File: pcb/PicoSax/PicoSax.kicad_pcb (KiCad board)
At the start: 2 copper layers, 100 x 160 mm, 80 parts, among them J3 Conn_01x02, M1 MountingHole_3.2mm_M3, M2 MountingHole_3.2mm_M3, M3 MountingHole_3.2mm_M3, M4 MountingHole_3.2mm_M3, M5 MountingHole_3.2mm_M3, M6 MountingHole_3.2mm_M3, SW8va1 Omron_B3K_L13L, SW8vb1 Omron_B3K_L13L, U1 Perfboard

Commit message: Clean and Parts BOM
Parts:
- R16: footprint Resistor_THT:R_Axial_DIN0204_L3.6mm_D1.6mm_P7.62mm_Horizontal -> Resistor_SMD:R_1210_3225Metric_Pad1.30x2.65mm_HandSolder
- R17: footprint Resistor_THT:R_Axial_DIN0204_L3.6mm_D1.6mm_P7.62mm_Horizontal -> Resistor_SMD:R_0805_2012Metric_Pad1.20x1.40mm_HandSolder
- moved R16 20.9 mm to (138.0, 187.0), turned to -90 degrees
- moved R17 3.31 mm to (123.0, 201.5)
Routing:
- net +3V3: track 450.2 -> 441.0 mm, vias 1 -> 2
- net Net-(J2-Vref): track 9.94 -> 4.78 mm
- net Net-(A1-GPIO0): track 14.7 -> 17.2 mm
- net Net-(J2-Data): track 9.94 -> 12.2 mm

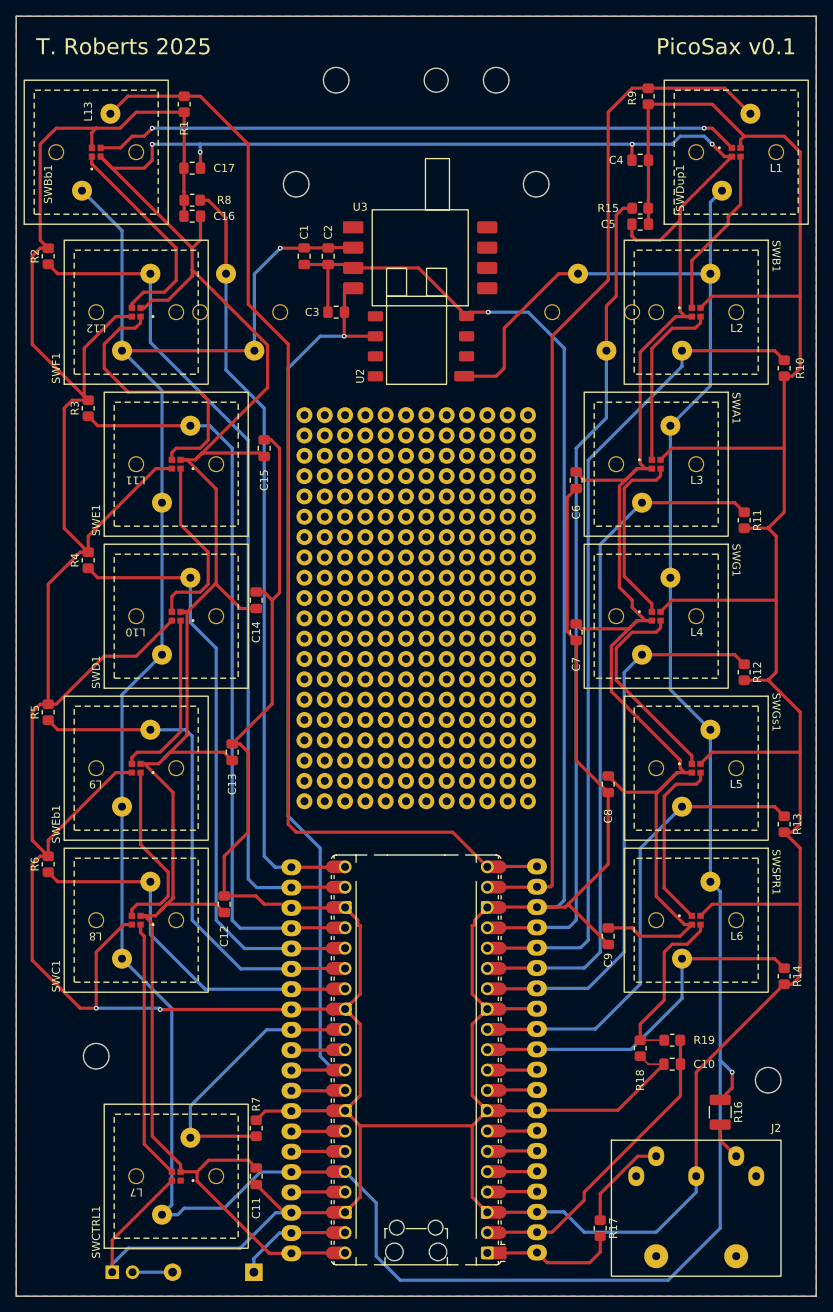
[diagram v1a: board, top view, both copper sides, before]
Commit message: v0.2
Updated LED footprint to have correct pin numbering.  Redid layout and traces. Added helpful silkscreen for pi pico.  Added some datasheets.
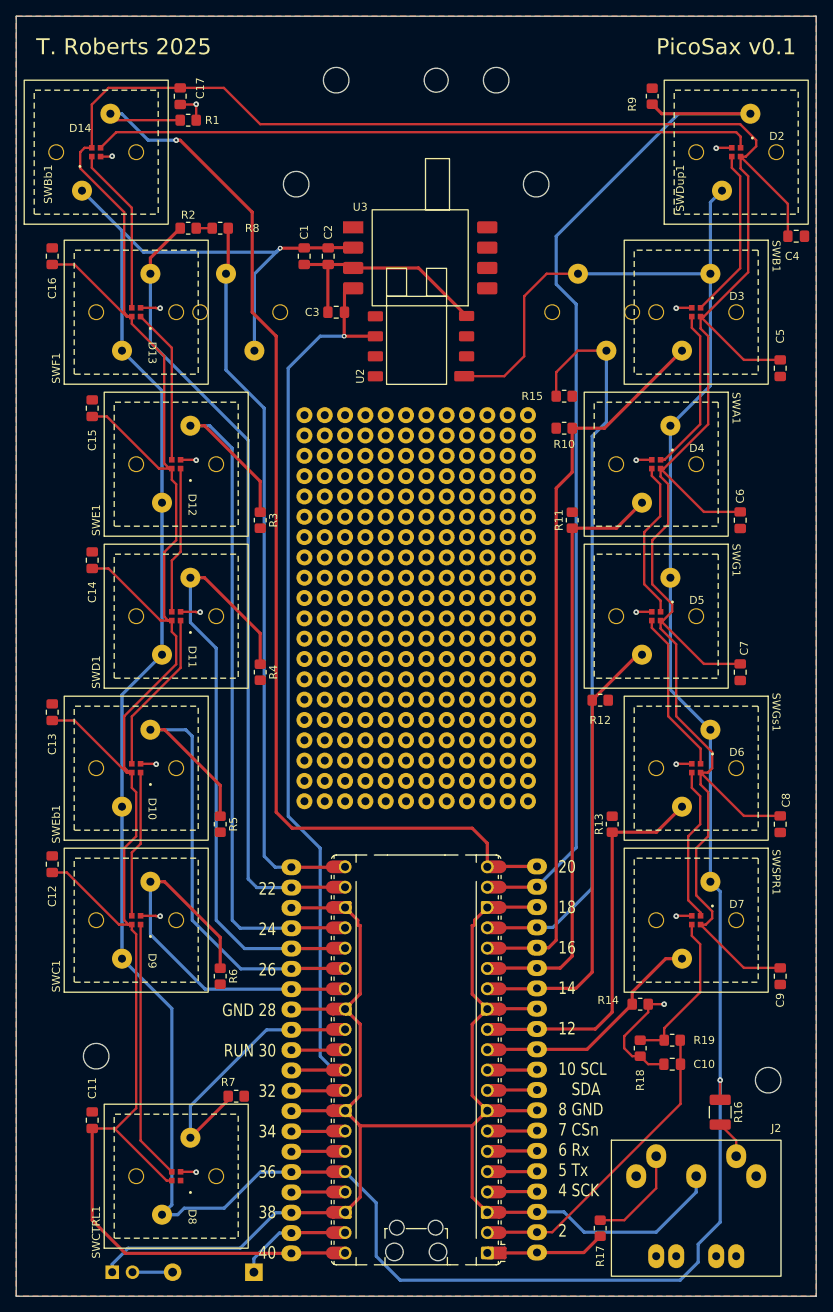
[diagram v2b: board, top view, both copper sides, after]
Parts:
- D10: renamed from L9; footprint MyLibrary:19-C47&slash_RSGHBHC-5V01&slash_2T_EVE-M -> PicoSax:19-C47_RSGHBHC-5V01-2T
- D11: renamed from L10; footprint MyLibrary:19-C47&slash_RSGHBHC-5V01&slash_2T_EVE-M -> PicoSax:19-C47_RSGHBHC-5V01-2T
- D12: renamed from L11; footprint MyLibrary:19-C47&slash_RSGHBHC-5V01&slash_2T_EVE-M -> PicoSax:19-C47_RSGHBHC-5V01-2T
- D13: renamed from L12; footprint MyLibrary:19-C47&slash_RSGHBHC-5V01&slash_2T_EVE-M -> PicoSax:19-C47_RSGHBHC-5V01-2T
- D14: renamed from L13; footprint MyLibrary:19-C47&slash_RSGHBHC-5V01&slash_2T_EVE-M -> PicoSax:19-C47_RSGHBHC-5V01-2T
- D2: renamed from L1; footprint MyLibrary:19-C47&slash_RSGHBHC-5V01&slash_2T_EVE-M -> PicoSax:19-C47_RSGHBHC-5V01-2T
- D3: renamed from L2; footprint MyLibrary:19-C47&slash_RSGHBHC-5V01&slash_2T_EVE-M -> PicoSax:19-C47_RSGHBHC-5V01-2T
- D4: renamed from L3; footprint MyLibrary:19-C47&slash_RSGHBHC-5V01&slash_2T_EVE-M -> PicoSax:19-C47_RSGHBHC-5V01-2T
- D5: renamed from L4; footprint MyLibrary:19-C47&slash_RSGHBHC-5V01&slash_2T_EVE-M -> PicoSax:19-C47_RSGHBHC-5V01-2T
- D6: renamed from L5; footprint MyLibrary:19-C47&slash_RSGHBHC-5V01&slash_2T_EVE-M -> PicoSax:19-C47_RSGHBHC-5V01-2T
- D7: renamed from L6; footprint MyLibrary:19-C47&slash_RSGHBHC-5V01&slash_2T_EVE-M -> PicoSax:19-C47_RSGHBHC-5V01-2T
- D8: renamed from L7; footprint MyLibrary:19-C47&slash_RSGHBHC-5V01&slash_2T_EVE-M -> PicoSax:19-C47_RSGHBHC-5V01-2T
- D9: renamed from L8; footprint MyLibrary:19-C47&slash_RSGHBHC-5V01&slash_2T_EVE-M -> PicoSax:19-C47_RSGHBHC-5V01-2T
- J2: footprint MyLibrary:MIDI_DIN5 -> PicoSax:MIDI_DIN5
- moved R10 28.5 mm to (118.5, 101.5), turned to 180 degrees
- moved R3 25.7 mm to (80.5, 113.0), turned to -90 degrees
- moved R4 25.7 mm to (80.5, 132.0), turned to -90 degrees
- moved R5 25.7 mm to (75.5, 151.0), turned to -90 degrees
- moved R6 25.7 mm to (75.5, 170.0), turned to -90 degrees
- moved R15 25.3 mm to (118.5, 97.5)
- moved C5 25.1 mm to (145.5, 94.0), turned to -90 degrees
- moved C13 23.0 mm to (54.5, 137.0)
- moved C12 22.1 mm to (54.5, 156.0)
- moved C15 22.1 mm to (59.5, 99.0)
- moved C8 22.1 mm to (145.5, 151.0)
- moved C9 22.1 mm to (145.5, 170.0)
- moved C4 21.7 mm to (147.5, 77.5)
- moved C11 21.7 mm to (59.5, 188.0), turned to 90 degrees
- moved R11 21.5 mm to (119.5, 113.0), turned to 90 degrees
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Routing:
- net GND: track 1029.9 -> 278.9 mm, vias 3 -> 15
- net +5V: track 498.5 -> 538.0 mm, vias 4 -> 0
- net Net-(D12-DIn): track 35.2 -> 19.5 mm
- net /Spr: track 45.2 -> 29.9 mm
- net /G: track 70.4 -> 56.6 mm
- net /B: track 104.8 -> 91.6 mm
- net /A: track 86.6 -> 74.8 mm
- net /8va: track 104.1 -> 93.5 mm
- net /Gs: track 59.1 -> 49.0 mm
- net Net-(D13-DIn): track 27.1 -> 21.0 mm
- net /F: track 106.6 -> 100.5 mm
- net /Dup: track 128.1 -> 134.0 mm
- net Net-(D5-DIn): track 25.9 -> 20.4 mm
- net /8vb: track 96.6 -> 91.3 mm
- net Net-(D11-DIn): track 23.0 -> 18.4 mm
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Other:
- board text added: "20 18 16 14 12 10 SCL SDA 8 GND 7 CSn 6 Rx 5 Tx 4 SCK 2"
- board text added: "22 24 26 GND 28 RUN 30 32 34 36 38 40"

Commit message: v0.2 Silkscreen
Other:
- board text added: "PicoSax v0.2"
- board text removed: "PicoSax v0.1"
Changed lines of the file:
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@@
 		)
 		(group ""
-			(members "086fbb49-340c-4092-ac16-3b2fb377506b" "0a748075-0325-4b25-ae1c-3b1340523989"
-				"0d9e2712-da3d-46ba-941b-578c9ca9716c" "0ec12be3-4299-4eed-8999-63e04e5bf408"
-				"14a3973c-bdbb-4f0b-ab51-99a944f14e3e" "170240d3-fe36-4ea2-aa65-822ce0f79894"
-				"248369f5-9f03-40ea-9894-73d1c22f1eb1" "2769e762-5a5d-4509-b222-9d5381171c7f"
-				"289c9828-77ef-4c7b-af1b-91fe4cccb365" "33c5214b-91d3-4bb3-9e43-7ec0733ebdd1"
-				"3e696417-7c9f-4e13-a6cd-ef270a2be7b6" "3f76528c-e8b3-4a1b-8cd7-3c9018933f79"
-				"40fea327-c866-45ed-9e40-b74438490b45" "4447463b-c720-4ec7-bba4-d10f0006f087"
-				"4be8b8df-a1cf-4da1-a25b-0f428821f060" "4d750b4a-1d82-4a57-a198-2df9849864f4"
-				"4d9647c7-de3c-47eb-9cef-4c4329a06382" "503569ec-f38e-41fd-9da8-a40785697783"
-				"54137541-2ff5-4156-8561-277d4b1860de" "56452df0-3793-4f6e-a38a-697a60366b47"
-				"5b9ee21b-1fea-46f3-b042-433d96bef95c" "60c96f77-5977-4711-baa9-736da1819767"
-				"6398b5f7-4add-428c-a507-9e618a09b480" "7085014e-72e0-4125-83da-d3b098a96abc"
-				"80594243-740f-4f1b-9363-dd562a7afe8a" "8bdffc08-4f19-4167-9494-c7daa5d9dd6e"
-				"8c683222-ecae-4a6d-a243-7c2dc7efff21" "8d99eefa-dd62-4b80-9d0e-75e5e37bdcdd"
-				"9aed28ff-c19e-4012-900c-070ae005ab42" "9af7f3ec-2d6b-43ff-a139-916a5a7395cc"
-				"9b064802-be43-4997-8182-7c9f972b9e79" "a5f9b0f7-63f7-41f4-bb60-1ae81ea60400"
-				"b00e83cc-4dd9-4ec2-87f4-2ec63945b012" "bddd0c79-6914-4cd3-b7e1-5f6f926488bf"
-				"c8f31c3e-e067-462c-b37f-ecec6f1ce858" "cb819c15-e7df-4ca2-8b22-6a7a1858fb93"
-				"d18fe79f-21fa-456b-97f7-b86b6fc3217a" "ddef6eee-512b-46bc-ac8e-7605d60f2b34"
-				"e277d9b8-fa04-4c39-99f8-5f855f8691c6" "e882dc5c-5fe6-4eba-8a98-0ab16f5c633a"
-				"e9d9d8c0-7030-4c00-acf4-5d9ab202e600" "eb0569bd-4187-4b98-8c4f-fb153d72eacf"
-				"ed551a5c-b073-43c5-9a28-df3dba0d35ab" "f1a64061-988b-4cb4-83e3-6c89f19fb58b"
-				"f3755e70-bf1c-45a8-b774-8f128797788a" "f74f5067-8940-4ee6-b594-05108584752e"
-				"f883a951-2930-40b7-8f3a-b64df69e0cfc" "fcecb49e-15f6-498d-adc9-82b7929b87a8"
-			)
-		)
-		(group ""
-			(members "0dfa6f0c-d96c-4c15-9d40-9307cf0acaf8" "1f269a71-376d-4267-bcaf-e124a14d4f1a"
-				"3366d0ed-e0c7-4618-af66-3a9920fa8abc" "369f357f-3c73-48ee-b1d9-4a2c1381d4b6"
-				"473abd8e-769c-4bb9-a4e9-b8062483d0df" "5cae54b6-ead8-47ad-8059-047de7cd318b"
-				"621a164e-f9d4-4e92-af63-c6ef2c5eeb81" "62587bbc-7df0-400b-af10-01b4adb5f2bf"
-				"790c9925-8b04-4a0d-b4ad-d7ccd3edc333" "814d9836-6b26-4b5f-babc-7e3aa374dca8"
-				"83ee131c-baf6-45b0-a961-c326a8d426d5" "8478b01e-935e-4d0c-bc6d-8d94a3b51a82"
-				"8b57397b-aa09-47d6-8941-ed0fe9d304c0" "8df7fa84-caf1-4d86-a20b-ff41820abee2"
-				"909b767e-bd7f-4e72-9072-c8ff5f8d2dfb" "94d98e94-029a-429d-9804-492ef8209813"
-				"a0af8e8c-045e-4797-889c-f621b26a09d3" "a3caeba2-1f38-4159-8037-493ff2e50467"
-				"adc18a67-06d6-4bc2-ba0f-eb59b7a19c8c" "bea10445-694b-472f-9fca-e11192d6843f"
-				"bf364228-297f-4708-821d-deed4ec923e8" "c927ae34-6fd4-4640-a8b1-c7a679167065"
-				"d3680f79-efe0-4da4-92c1-95a83297d465" "df88a17f-874f-4b78-8925-7a6206d8fe96"
-				"e28308e2-363d-4ca6-b2f3-625a79248a9e" "f2ad7ec6-706c-4df0-883f-0097e59067e2"
-				"f6f680ac-7f31-4a62-8373-1c89685b5431" "f995f8f5-e358-4011-abc7-d3857e707559"
-			)
-		)
-		(group ""
 			(members "064e17c1-038d-4744-b373-d8a1aa759853" "06516e1e-dc13-4ecc-8d61-0a5ac7f1273b"
 				"086fbb49-340c-4092-ac16-3b2fb377506b" "0a748075-0325-4b25-ae1c-3b1340523989"
@@
 		)
 		(group ""
+			(members "0dfa6f0c-d96c-4c15-9d40-9307cf0acaf8" "1f269a71-376d-4267-bcaf-e124a14d4f1a"
+				"3366d0ed-e0c7-4618-af66-3a9920fa8abc" "369f357f-3c73-48ee-b1d9-4a2c1381d4b6"
+				"473abd8e-769c-4bb9-a4e9-b8062483d0df" "5cae54b6-ead8-47ad-8059-047de7cd318b"
+				"621a164e-f9d4-4e92-af63-c6ef2c5eeb81" "62587bbc-7df0-400b-af10-01b4adb5f2bf"
+				"790c9925-8b04-4a0d-b4ad-d7ccd3edc333" "814d9836-6b26-4b5f-babc-7e3aa374dca8"
+				"83ee131c-baf6-45b0-a961-c326a8d426d5" "8478b01e-935e-4d0c-bc6d-8d94a3b51a82"
+				"8b57397b-aa09-47d6-8941-ed0fe9d304c0" "8df7fa84-caf1-4d86-a20b-ff41820abee2"
+				"909b767e-bd7f-4e72-9072-c8ff5f8d2dfb" "94d98e94-029a-429d-9804-492ef8209813"
+				"a0af8e8c-045e-4797-889c-f621b26a09d3" "a3caeba2-1f38-4159-8037-493ff2e50467"
+				"adc18a67-06d6-4bc2-ba0f-eb59b7a19c8c" "bea10445-694b-472f-9fca-e11192d6843f"
+				"bf364228-297f-4708-821d-deed4ec923e8" "c927ae34-6fd4-4640-a8b1-c7a679167065"
+				"d3680f79-efe0-4da4-92c1-95a83297d465" "df88a17f-874f-4b78-8925-7a6206d8fe96"
+				"e28308e2-363d-4ca6-b2f3-625a79248a9e" "f2ad7ec6-706c-4df0-883f-0097e59067e2"
+				"f6f680ac-7f31-4a62-8373-1c89685b5431" "f995f8f5-e358-4011-abc7-d3857e707559"
+			)
+		)
+		(group ""
 			(members "0cc3ed1f-3e1a-4ab2-abcb-f182e4cc6d60" "2d84d8c6-271b-42db-be9e-6d1802cfc7d3"
 				"2e832cae-8d56-4461-8eab-4c332c6a8012" "2e905759-b6a6-484c-b1ef-c5e89f1340af"
@@
 		)
 		(group ""
+			(members "0d9e2712-da3d-46ba-941b-578c9ca9716c" "4447463b-c720-4ec7-bba4-d10f0006f087"
+				"6398b5f7-4add-428c-a507-9e618a09b480" "7085014e-72e0-4125-83da-d3b098a96abc"
+				"9b064802-be43-4997-8182-7c9f972b9e79" "a5f9b0f7-63f7-41f4-bb60-1ae81ea60400"
+				"bddd0c79-6914-4cd3-b7e1-5f6f926488bf" "f883a951-2930-40b7-8f3a-b64df69e0cfc"
+			)
+		)
+		(group ""
 			(members "172120e8-e440-4bff-83df-04c20516cd6e" "1b1d152a-5ae1-4272-a8b5-21354d0f552a"
 				"43b77187-18fe-4779-aebd-4fc34a05e8c2" "57465056-415f-4c0b-b1e8-babd4fb4937a"
@@
 		)
 	)
-	(gr_text "PicoSax v0.1"
+	(gr_text "PicoSax v0.2"
 		(at 147.5 55 0)
 		(layer "F.SilkS")

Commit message: move air pressure
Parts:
- U1: footprint MyLibrary:Perfboard 12x20 -> MyLibrary:Perfboard 10x20
- moved C1 53.0 mm to (87.5, 133.0)
- moved C2 53.0 mm to (90.5, 133.0)
- moved C3 53.0 mm to (91.5, 140.0)
- moved U2 53.0 mm to (107.8, 143.0)
- moved U3 53.0 mm to (93.6, 129.4)
- moved U1 23.5 mm to (88.8, 76.5)
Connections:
- U1 pad : (no net) -> GND
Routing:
- net +3V3: track 444.2 -> 534.8 mm, vias 2 -> 1
- net Net-(A1-GPIO26_ADC0): track 117.0 -> 59.6 mm
- net GND: track 278.9 -> 250.0 mm
- net /Bb: track 145.3 -> 147.4 mm

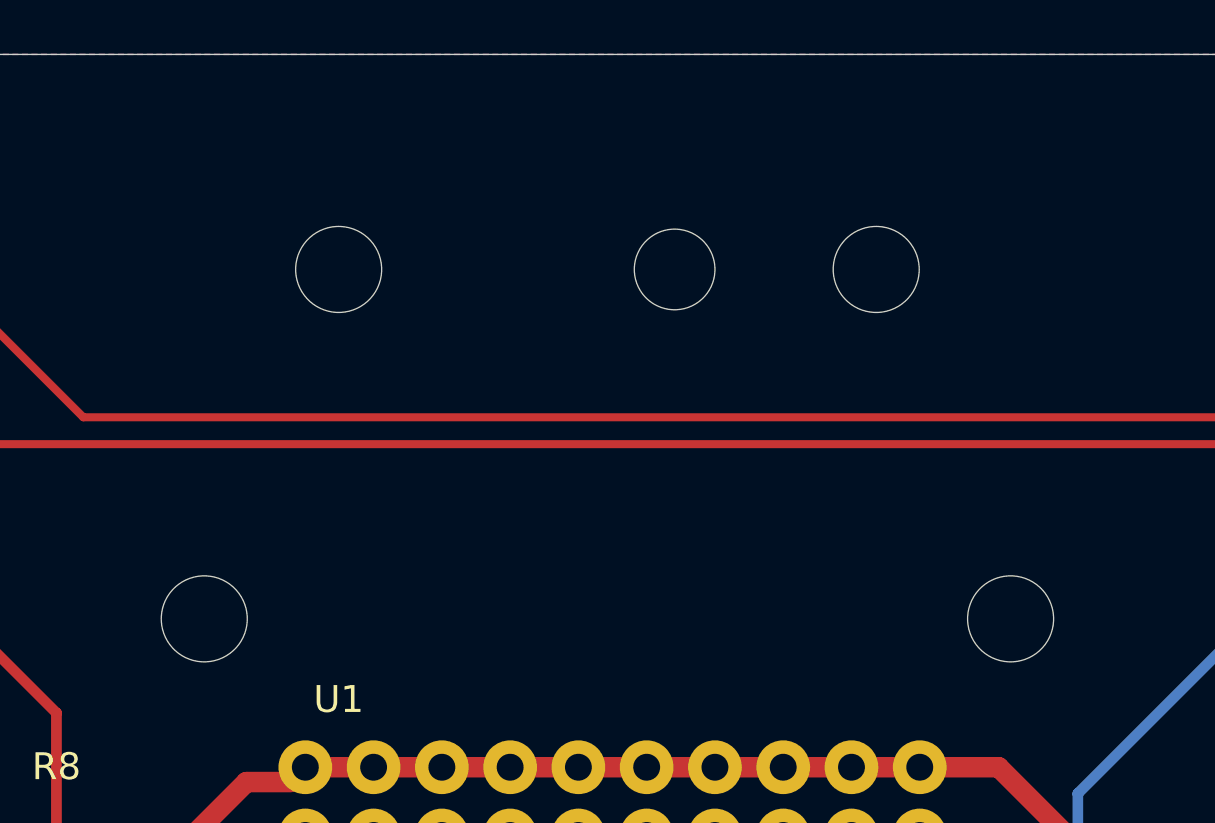
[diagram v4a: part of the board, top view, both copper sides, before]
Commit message: Mouthpiece mounting hole update
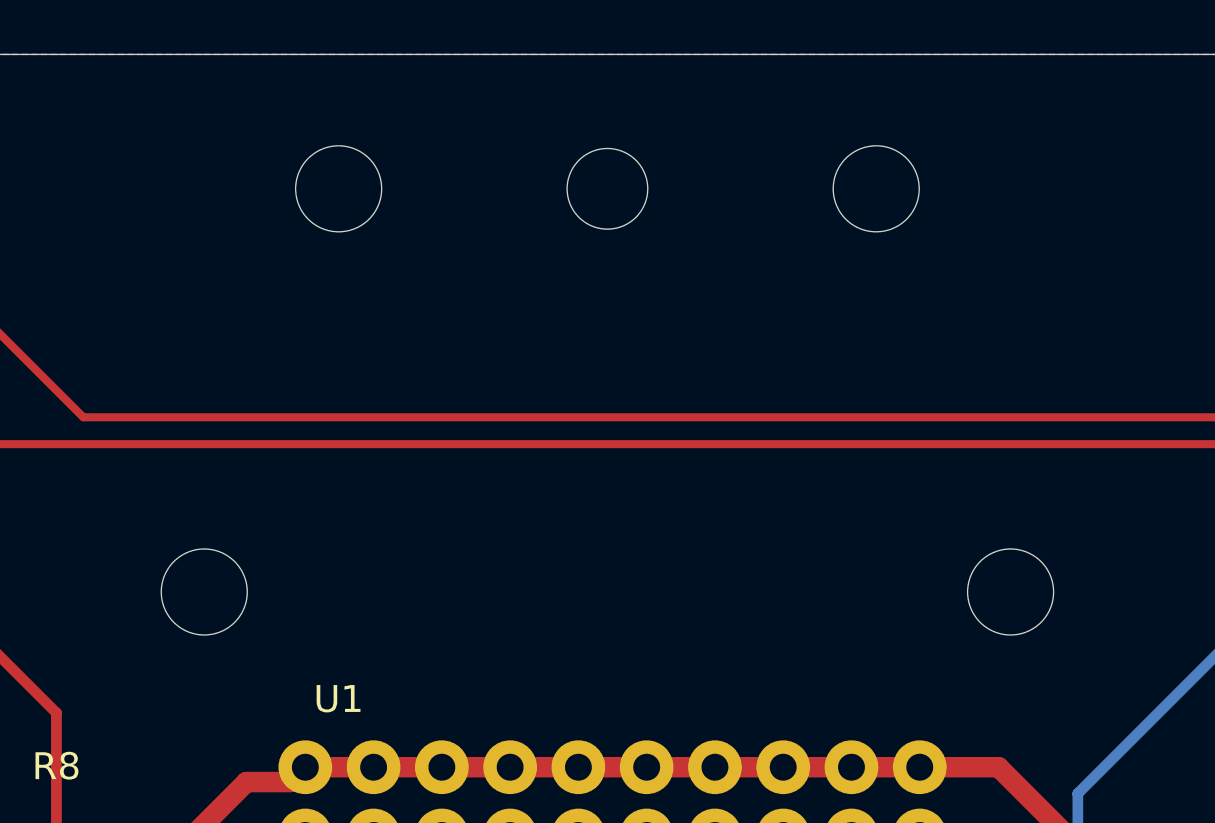
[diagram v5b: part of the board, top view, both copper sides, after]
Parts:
- moved REF** 3.91 mm to (100.0, 55.0)
- moved M1 3.00 mm to (90.0, 55.0)
- moved M2 3.00 mm to (110.0, 55.0)
- moved M3 1.00 mm to (85.0, 70.0)
- moved M4 1.00 mm to (115.0, 70.0)
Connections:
- U1 pad : GND -> (no net)
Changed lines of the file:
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@@
 	(footprint "MountingHole:MountingHole_3.2mm_M3"
 		(layer "F.Cu")
-		(at 115 71)
+		(at 115 70)
 		(descr "Mounting Hole 3.2mm, no annular, M3")
 		(tags "mounting hole 3.2mm no annular m3")
@@
 			(layers "*.Cu" "*.Mask")
 			(remove_unused_layers no)
-			(net 31 "+3V3")
 		)
 		(pad "" thru_hole circle
@@
 			(layers "*.Cu" "*.Mask")
 			(remove_unused_layers no)
-			(net 4 "GND")
 		)
 		(pad "" thru_hole circle
@@
 			(layers "*.Cu" "*.Mask")
 			(remove_unused_layers no)
-			(net 31 "+3V3")
 		)
 		(pad "" thru_hole circle
@@
 			(layers "*.Cu" "*.Mask")
 			(remove_unused_layers no)
-			(net 4 "GND")
 		)
 		(pad "" thru_hole circle
@@
 			(layers "*.Cu" "*.Mask")
 			(remove_unused_layers no)
-			(net 31 "+3V3")
 		)
 		(pad "" thru_hole circle
@@
 			(layers "*.Cu" "*.Mask")
 			(remove_unused_layers no)
-			(net 4 "GND")
 		)
 		(pad "" thru_hole circle
@@
 			(layers "*.Cu" "*.Mask")
 			(remove_unused_layers no)
-			(net 31 "+3V3")
 		)
 		(pad "" thru_hole circle
@@
 			(layers "*.Cu" "*.Mask")
 			(remove_unused_layers no)
-			(net 4 "GND")
 		)
 		(pad "" thru_hole circle
@@
 			(layers "*.Cu" "*.Mask")
 			(remove_unused_layers no)
-			(net 31 "+3V3")
 		)
 		(pad "" thru_hole circle
@@
 			(layers "*.Cu" "*.Mask")
 			(remove_unused_layers no)
-			(net 4 "GND")
 		)
 		(pad "" thru_hole circle
@@
 			(layers "*.Cu" "*.Mask")
 			(remove_unused_layers no)
-			(net 31 "+3V3")
 		)
 		(pad "" thru_hole circle
@@
 			(layers "*.Cu" "*.Mask")
 			(remove_unused_layers no)
-			(net 4 "GND")
 		)
 		(pad "" thru_hole circle
@@
 			(layers "*.Cu" "*.Mask")
 			(remove_unused_layers no)
-			(net 31 "+3V3")
 		)
 		(pad "" thru_hole circle
@@
 			(layers "*.Cu" "*.Mask")
 			(remove_unused_layers no)
-			(net 4 "GND")
 		)
 		(pad "" thru_hole circle
@@
 			(layers "*.Cu" "*.Mask")
 			(remove_unused_layers no)
-			(net 31 "+3V3")
 		)
 		(pad "" thru_hole circle
@@
 			(layers "*.Cu" "*.Mask")
 			(remove_unused_layers no)
-			(net 4 "GND")
 		)
 		(pad "" thru_hole circle
@@
 			(layers "*.Cu" "*.Mask")
 			(remove_unused_layers no)
-			(net 31 "+3V3")
 		)
 		(pad "" thru_hole circle
@@
 			(layers "*.Cu" "*.Mask")
 			(remove_unused_layers no)
-			(net 4 "GND")
 		)
 		(pad "1" thru_hole circle
@@
 	(footprint "MountingHole:MountingHole_3.2mm_M3"
 		(layer "F.Cu")
-		(at 85 71)
+		(at 85 70)
 		(descr "Mounting Hole 3.2mm, no annular, M3")
 		(tags "mounting hole 3.2mm no annular m3")
@@
 	(footprint "MountingHole:MountingHole_3.2mm_M3"
 		(layer "F.Cu")
-		(at 110 58)
+		(at 110 55)
 		(descr "Mounting Hole 3.2mm, no annular, M3")
 		(tags "mounting hole 3.2mm no annular m3")
@@
 	(footprint "MountingHole:MountingHole_3mm"
 		(layer "F.Cu")
-		(at 102.5 58)
+		(at 100 55)
 		(descr "Mounting Hole 3mm, no annular")
 		(tags "mounting hole 3mm no annular")
@@
 	(footprint "MountingHole:MountingHole_3.2mm_M3"
 		(layer "F.Cu")
-		(at 90 58)
+		(at 90 55)
 		(descr "Mounting Hole 3.2mm, no annular, M3")
 		(tags "mounting hole 3.2mm no annular m3")
